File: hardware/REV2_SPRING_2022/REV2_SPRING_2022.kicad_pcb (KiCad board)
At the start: 2 copper layers, 108 x 304.8 mm, 52 parts, among them J101 Screw_Terminal_01x02, J102 Screw_Terminal_01x02, J103 Conn_01x02_Female, J104 Screw_Terminal_01x02, J105 Conn_01x02_Female, J107 Screw_Terminal_01x02, J109 Conn_01x02_Female, J110 Conn_01x02_Female, Q101 Q_NMOS_GDS, Q102 Q_NMOS_GDS, U1 Teensy3.6_All_Pins, U2 PA16165_Breakout, U201 TPS2113ADRBR, U3 MPL3115A2_Breakout, U301 TPS2113ADRBR, U4 BNO055_Breakout, U5 RFM69HCW_Breakout

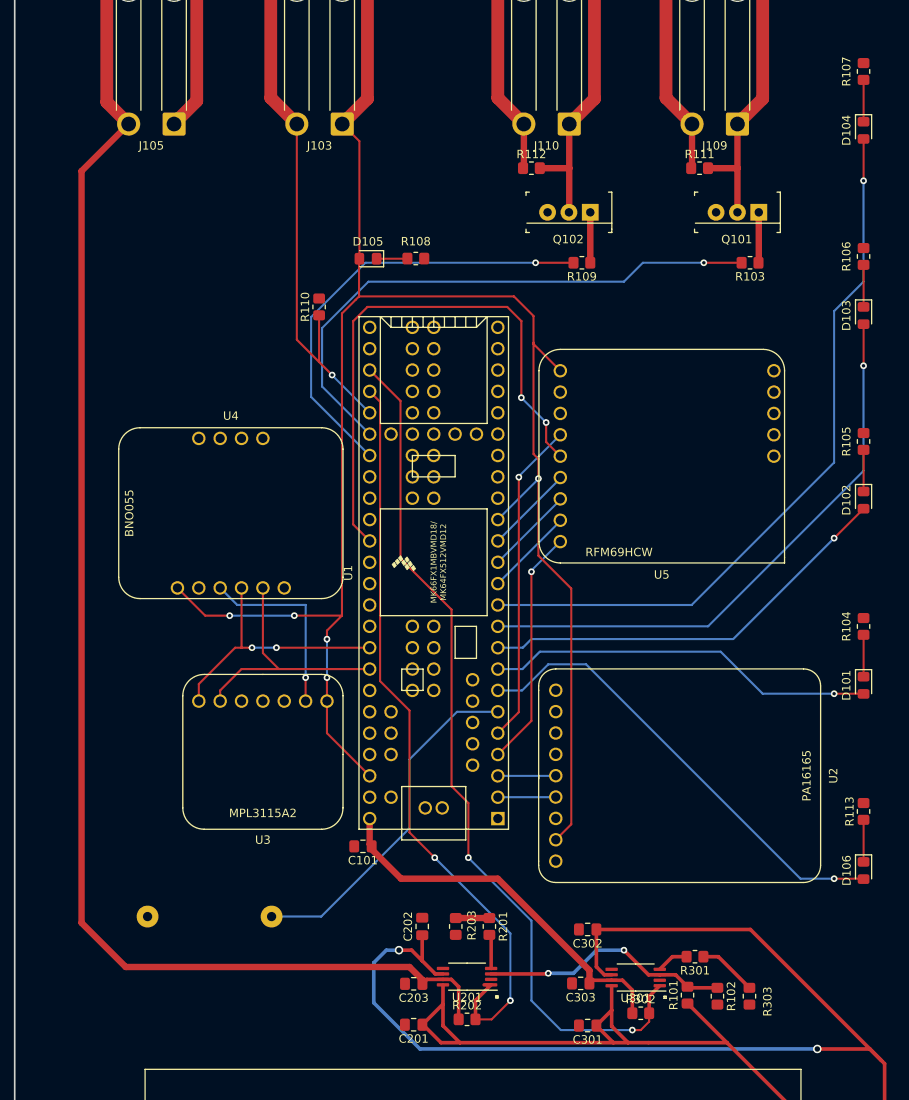
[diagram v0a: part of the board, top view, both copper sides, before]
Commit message: move buzzer
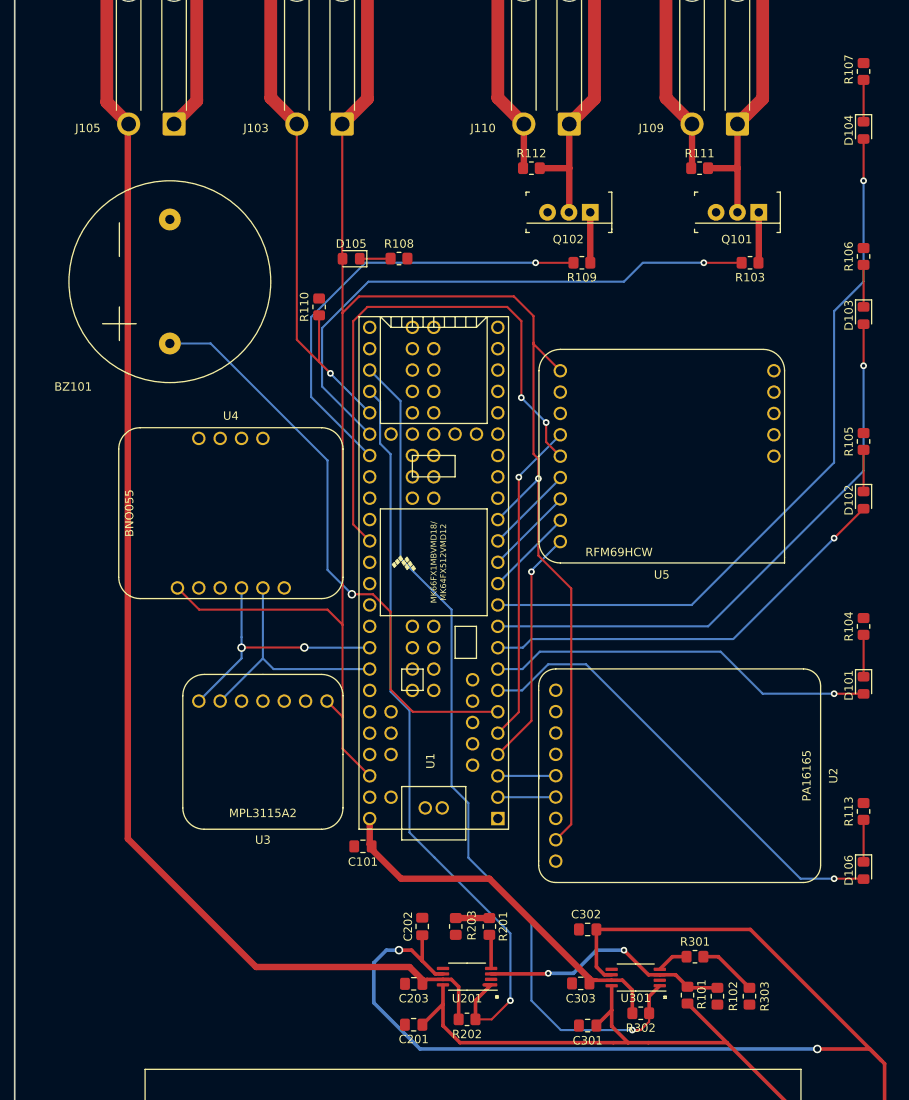
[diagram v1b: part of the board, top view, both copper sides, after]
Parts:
- BZ101: moved to F.Cu
- moved BZ101 75.6 mm to (78.5, 85.0), turned to 90 degrees
- moved D105 2.00 mm to (100.1, 82.3)
- moved R108 2.00 mm to (105.8, 82.2)
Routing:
- net /BUZZER: track 41.8 -> 70.2 mm, vias 0 -> 1
- net GND: track 89.0 -> 66.6 mm, vias 1 -> 0
- net /V_EMATCH_TO_KEY_SWITCH: track 194.1 -> 180.5 mm
- net /BAT1: track 85.6 -> 77.5 mm
- net /3.3V: track 245.6 -> 248.3 mm, vias 5 -> 1
- net /SCL0: track 30.5 -> 28.8 mm
- net /TPS_2_STAT: vias 2 -> 1
- net /TPS_1_STAT: vias 2 -> 1

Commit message: finish layout
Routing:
- net /BAT2: track 164.2 -> 162.8 mm
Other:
- board size 108 x 304.8 mm -> 105 x 250 mm
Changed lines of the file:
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@@
     (thickness 1.6)
     (drawings 26)
-    (tracks 335)
+    (tracks 336)
     (zones 0)
     (modules 52)
@@
   )
   (setup
-    (last_trace_width 0.25)
+    (last_trace_width 0.4318)
     (user_trace_width 0.4318)
     (user_trace_width 0.762)
@@
     )
   )
+  (gr_circle (center 156.25 234.25) (end 158.75 234.25) (layer Edge.Cuts) (width 0.2))
+  (gr_circle (center 156.249999 4.25) (end 158.749999 4.25) (layer Edge.Cuts) (width 0.2))
+  (gr_circle (center 71.25 4.25) (end 73.75 4.25) (layer Edge.Cuts) (width 0.2))
+  (gr_circle (center 71.25 234.25) (end 73.75 234.25) (layer Edge.Cuts) (width 0.2))
+  (gr_line (start 61.250001 244.25) (end 166.25 244.25) (layer Edge.Cuts) (width 0.2))
+  (gr_line (start 61.25 -5.75) (end 61.250001 244.25) (layer Edge.Cuts) (width 0.2))
+  (gr_line (start 166.249999 -5.75) (end 166.25 244.25) (layer Edge.Cuts) (width 0.2))
+  (gr_line (start 61.25 -5.75) (end 166.249999 -5.75) (layer Edge.Cuts) (width 0.2))
   (gr_text "KEY SWITCH\nWIRES 1 & 2" (at 75 18) (layer B.SilkS)
     (effects (font (size 1.5 1.5) (thickness 0.3)) (justify mirror))
@@
     (effects (font (size 1.5 1.5) (thickness 0.3)))
   )
-  (gr_line (start 168 -65.25) (end 167.999999 239.55) (layer Edge.Cuts) (width 0.2))
-  (gr_circle (center 70.050001 -55.25) (end 72.550001 -55.25) (layer Edge.Cuts) (width 0.2))
-  (gr_circle (center 70.050001 229.55) (end 72.550001 229.55) (layer Edge.Cuts) (width 0.2))
-  (gr_line (start 60.05 239.55) (end 167.999999 239.55) (layer Edge.Cuts) (width 0.2))
-  (gr_line (start 60.050001 -65.25) (end 168 -65.25) (layer Edge.Cuts) (width 0.2))
-  (gr_circle (center 158 229.55) (end 160.5 229.55) (layer Edge.Cuts) (width 0.2))
-  (gr_line (start 60.050001 -65.25) (end 60.05 239.55) (layer Edge.Cuts) (width 0.2))
-  (gr_circle (center 158 -55.25) (end 160.5 -55.25) (layer Edge.Cuts) (width 0.2))
   (gr_line (start 117.274 170.188) (end 117.274 169.934) (angle 90) (layer F.SilkS) (width 0.12))
   (gr_line (start 117.528 170.188) (end 117.274 170.188) (angle 90) (layer F.SilkS) (width 0.12))
@@
   (segment (start 133 175.5) (end 131.04 173.54) (width 0.4318) (layer F.Cu) (net 121))
   (segment (start 131.04 167.4265) (end 130.1765 167.4265) (width 0.4318) (layer F.Cu) (net 122) (status 10))
-  (segment (start 129.225 166.475) (end 129.225 162.0365) (width 0.4318) (layer F.Cu) (net 122) (status 20))
   (segment (start 130.1765 167.4265) (end 129.225 166.475) (width 0.4318) (layer F.Cu) (net 122))
   (segment (start 110.9825 167.323) (end 110.073 167.323) (width 0.4318) (layer F.Cu) (net 122) (status 10))
   (segment (start 108.511 165.761) (end 108.511 162.7165) (width 0.4318) (layer F.Cu) (net 122) (status 20))
   (segment (start 110.073 167.323) (end 108.511 165.761) (width 0.4318) (layer F.Cu) (net 122))
-  (segment (start 129.225 162.0365) (end 147.5365 162.0365) (width 0.4318) (layer F.Cu) (net 122))
-  (segment (start 163.5 202.365) (end 155.555 210.31) (width 0.4318) (layer F.Cu) (net 122))
-  (segment (start 163.5 178) (end 163.5 202.365) (width 0.4318) (layer F.Cu) (net 122))
   (segment (start 108.511 165.761) (end 107.25 164.5) (width 0.4318) (layer F.Cu) (net 122))
   (via (at 105.75 164.5) (size 1.016) (drill 0.635) (layers F.Cu B.Cu) (net 122))
   (segment (start 107.25 164.5) (end 105.75 164.5) (width 0.4318) (layer F.Cu) (net 122))
   (via (at 155.5 176.25) (size 1.016) (drill 0.635) (layers F.Cu B.Cu) (net 122))
-  (segment (start 161.75 176.25) (end 163.125 177.625) (width 0.4318) (layer F.Cu) (net 122))
   (segment (start 155.5 176.25) (end 161.75 176.25) (width 0.4318) (layer F.Cu) (net 122))
-  (segment (start 163.125 177.625) (end 163.5 178) (width 0.4318) (layer F.Cu) (net 122))
-  (segment (start 147.5365 162.0365) (end 163.125 177.625) (width 0.4318) (layer F.Cu) (net 122))
   (segment (start 108.25 176.25) (end 155.5 176.25) (width 0.4318) (layer B.Cu) (net 122))
   (segment (start 102.75 170.75) (end 108.25 176.25) (width 0.4318) (layer B.Cu) (net 122))
@@
   (segment (start 104.25 164.5) (end 102.75 166) (width 0.4318) (layer B.Cu) (net 122))
   (segment (start 105.75 164.5) (end 104.25 164.5) (width 0.4318) (layer B.Cu) (net 122))
+  (segment (start 129.225 164.525) (end 129.225 162.0365) (width 0.4318) (layer F.Cu) (net 122))
+  (segment (start 129.225 166.475) (end 129.225 164.525) (width 0.4318) (layer F.Cu) (net 122))
+  (segment (start 163 202.865) (end 155.555 210.31) (width 0.4318) (layer F.Cu) (net 122))
+  (segment (start 163 177.75) (end 163 202.865) (width 0.4318) (layer F.Cu) (net 122))
+  (segment (start 163 177.5) (end 163 177.75) (width 0.4318) (layer F.Cu) (net 122))
+  (segment (start 147.5365 162.0365) (end 163 177.5) (width 0.4318) (layer F.Cu) (net 122))
+  (segment (start 131.7135 162.0365) (end 147.5365 162.0365) (width 0.4318) (layer F.Cu) (net 122))
+  (segment (start 129.225 164.525) (end 131.7135 162.0365) (width 0.4318) (layer F.Cu) (net 122))
   (segment (start 109.0645 167.973) (end 108.5375 168.5) (width 0.4318) (layer F.Cu) (net 123) (status 30))
   (segment (start 110.9825 167.973) (end 109.0645 167.973) (width 0.4318) (layer F.Cu) (net 123) (status 30))
@@
     (polygon
       (pts
-        (xy 172.72 243.84) (xy 55.88 243.84) (xy 55.88 -68.58) (xy 172.72 -68.58)
+        (xy 172.47 249.84) (xy 55.63 249.84) (xy 55.63 -62.58) (xy 172.47 -62.58)
       )
     )
@@
     (polygon
       (pts
-        (xy 172.72 243.84) (xy 55.88 243.84) (xy 55.88 -68.58) (xy 172.72 -68.58)
+        (xy 172.47 249.84) (xy 55.63 249.84) (xy 55.63 -62.58) (xy 172.47 -62.58)
       )
     )

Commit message: add logos
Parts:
- added G***: LOGO, Olin_Rocketry:Olin_Rocketry_Logo1, B.Cu at (78.0, 123.5)
- added G***: LOGO, Olin_Rocketry:Olin_O, B.Cu at (114.8, 205.0)
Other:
- board text added: "2022-01-29 Rev. 2 Ian Eykamp Charlie Babe Marc Eftimie Rowan Jansens"
- board text added: "Phoenix IV"

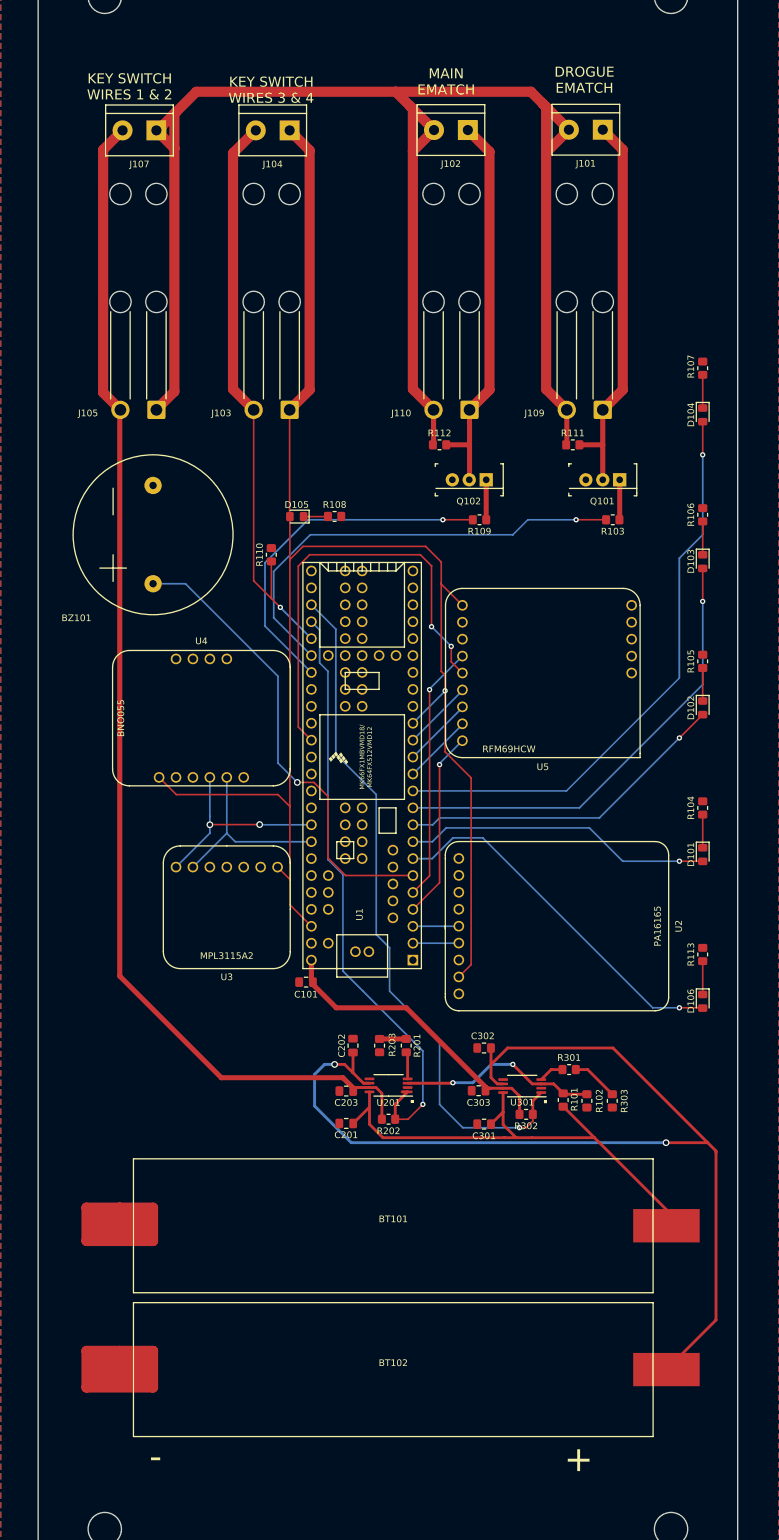
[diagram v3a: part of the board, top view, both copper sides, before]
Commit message: add vias
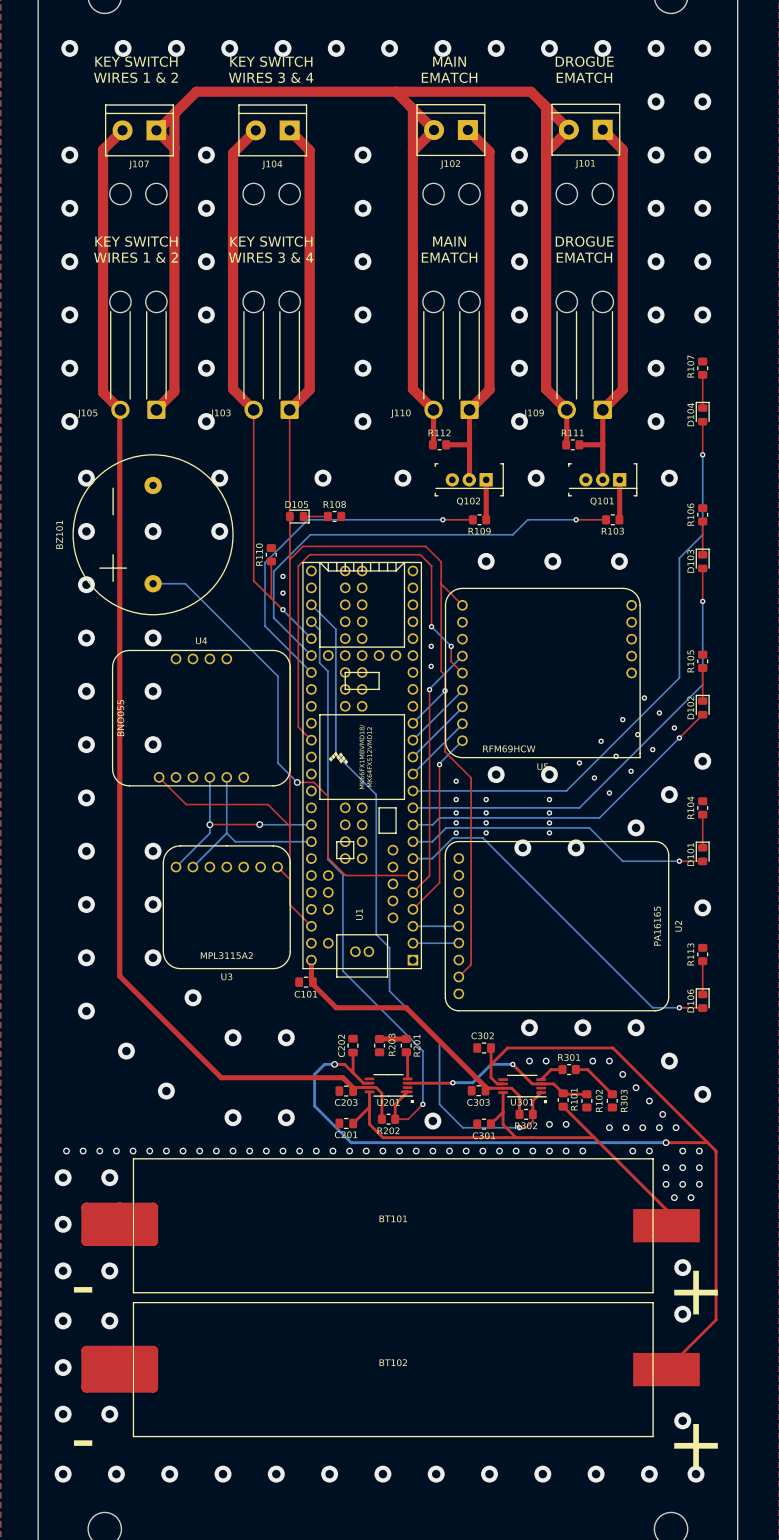
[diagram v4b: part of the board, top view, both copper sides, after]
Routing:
- net /3.3V: track 248.3 -> 249.5 mm
- net GND: vias 0 -> 211
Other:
- board text added: "2022-01-29 Rev. 2 Ian Eykamp Charlie Babe Marc Eftimie Rowan Jansens Abitamim Bharmal"
- board text removed: "2022-01-29 Rev. 2 Ian Eykamp Charlie Babe Marc Eftimie Rowan Jansens"
